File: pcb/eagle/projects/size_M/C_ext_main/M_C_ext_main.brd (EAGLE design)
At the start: 12 parts, among them U1 CP2104-F03-GM

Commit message: PCB M.1
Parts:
- added C.R3, C.R4: 0, rcl:R0603
- moved C.J2 0.29 mm to (1.64, 12.8)
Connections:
- net PROG: now also C.R4.1, C.R4.2
- net RESET: now also C.R3.1, C.R3.2
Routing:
- net PROG: track 9.97 -> 22.9 mm
- net GND: track 130.4 -> 128.3 mm
- net RX: track 5.99 -> 6.92 mm
- net VUSB: track 29.3 -> 30.1 mm
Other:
- board text added: "main M.1"
- board text removed: "ESP M.1"

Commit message: updated PCBS after the version 1 delivery
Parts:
- removed C.C4: 100n, rcl:C0603
- added C.R5: 5K1, rcl:R0603
- added C.R6: 5k1, rcl:R0603
- C.C5: value 10u -> 1u
- moved C.R3 4.08 mm to (14.9, 5.41)
- moved C.R2 3.87 mm to (3.90, 8.98)
- moved C.R1 2.03 mm to (3.87, 5.49)
- moved C.C5 1.82 mm to (3.95, 12.5)
- moved U1 1.78 mm to (11.1, 8.72)
- moved C.R4 1.11 mm to (7.86, 4.56)
- moved C.C2 0.44 mm to (17.2, 9.79)
- moved C.C3 0.14 mm to (18.7, 2.95)
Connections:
- removed net VIO: U1.5
- new net N$3: C.R6.2, U$1.A5
- new net N$4: C.R5.2, U$1.B5
- net GND: now also C.R5.1, C.R6.1; no longer C.C4.1
- net N$1: now also U$1.B7
- net N$2: now also U$1.B6
- net VCC: now also U1.5
- net VUSB: no longer C.C4.2
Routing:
- net N$2: track 2.25 -> 11.1 mm
- net VUSB: track 30.1 -> 38.7 mm
- net N$1: track 2.26 -> 9.99 mm, vias 0 -> 2
- net VCC: track 53.2 -> 46.2 mm
- net GND: track 128.3 -> 123.7 mm, vias 5 -> 9
- net N$3: track 0.00 -> 3.89 mm
- net N$4: track 0.00 -> 2.70 mm
- net SDA: track 6.33 -> 5.20 mm
- net RX: track 6.92 -> 5.81 mm
- net PROG: track 22.9 -> 24.0 mm
- net SCL: track 4.93 -> 5.89 mm
- net RESET: track 11.8 -> 12.7 mm
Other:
- board text added: "main M.2"
- board text removed: "main M.1"

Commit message: updated PCBs for version 2
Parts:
- added C.F1, C.F2: (no value), rcl:R0805
- added PROGRAMMING: TPB1,27, testpad:B1,27
- moved C.C2 4.30 mm to (14.9, 6.15)
- moved C.R3 3.91 mm to (11.1, 4.57)
- moved C.C1 0.76 mm to (19.0, 2.98)
- moved C.R5 0.38 mm to (13.1, 12.1)
- moved C.C3 0.33 mm to (18.7, 2.62)
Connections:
- new net N$5: C.F2.2, JP1.3
- new net N$6: C.F1.2, JP1.1
- new net N$7: PROGRAMMING.TP, U1.9
- net VCC: now also C.F2.1; no longer JP1.3
- net VUSB: now also C.F1.1; no longer JP1.1
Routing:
- net GND: track 123.7 -> 128.9 mm, vias 9 -> 8
- net VCC: track 46.2 -> 43.4 mm, vias 0 -> 2
- net N$6: track 0.00 -> 2.74 mm
- net N$5: track 0.00 -> 2.67 mm
- net VUSB: track 38.7 -> 36.0 mm
- net N$7: track 0.00 -> 1.62 mm
- net RESET: track 12.7 -> 11.2 mm

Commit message: closed PCB version M.2
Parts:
- renumbered PROGRAMMING to PROG

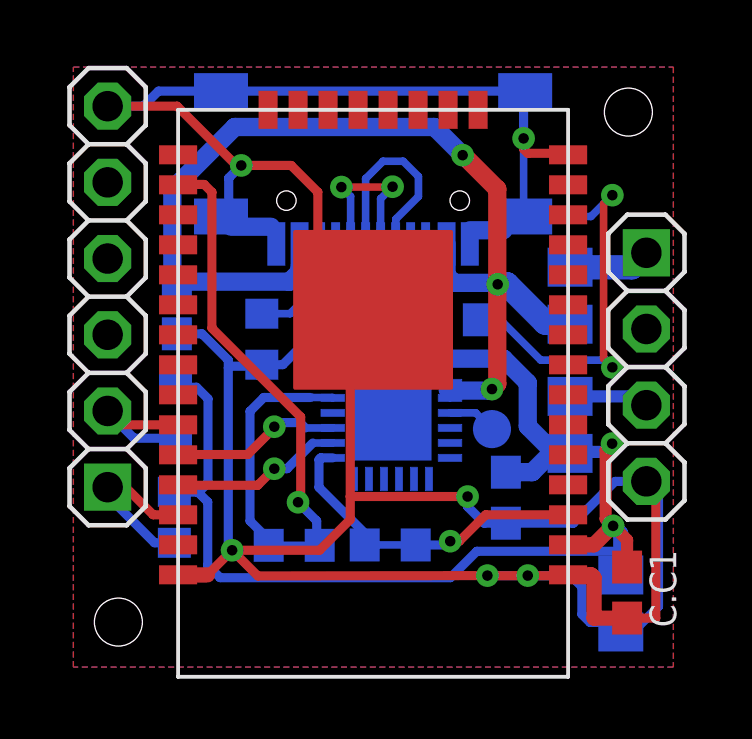
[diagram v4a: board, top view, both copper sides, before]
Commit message: updated main board - added 5 to 3.3V regulator becaues one in CP is too weak updated power board - added shotky diode to FET to be sure it works as expected
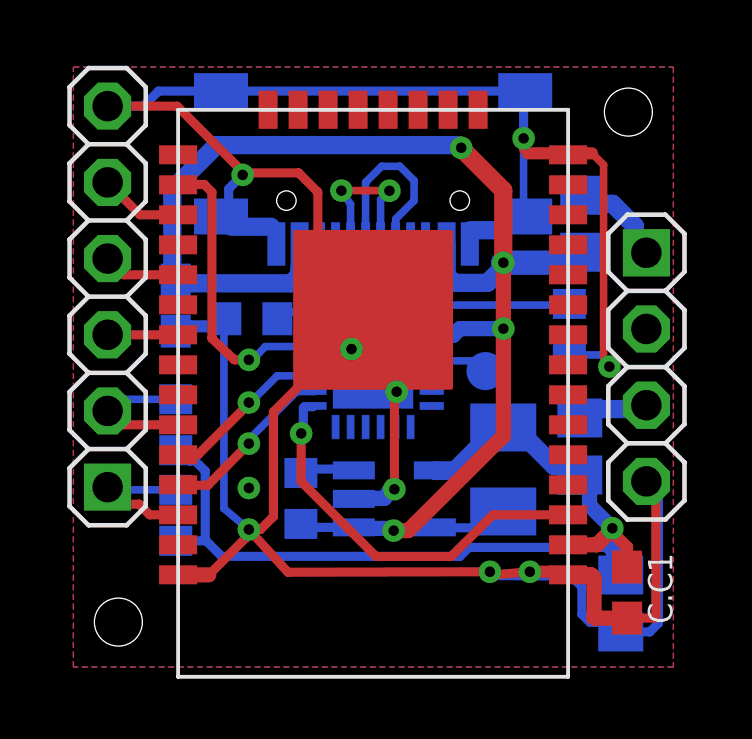
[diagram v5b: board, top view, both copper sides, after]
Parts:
- removed C.C2: 100n, rcl:C0603
- removed C.R4: 0, rcl:R0603
- removed PROG: TPB1,27, testpad:B1,27
- added D.L1: 2u2, rcl:L3230M
- added D.U2: LM3671_3.3, !stavebnice03:SOT32-5
- added P1: TPB1,27, testpad:B1,27
- C.F1, C.F2: value (none) -> 0.5A
- C.R3: value 0 -> 39k
- moved C.R5 3.91 mm to (17.0, 11.8), turned to 90 degrees
- moved C.R3 3.36 mm to (8.08, 6.12), turned to 270 degrees
- moved C.F1 2.44 mm to (17.5, 15.3)
- moved U1 1.84 mm to (10.5, 10.5)
- moved C.F2 0.79 mm to (17.4, 7.85)
- moved C.R6 0.76 mm to (6.45, 12.1), turned to 180 degrees
- moved C.R2 0.40 mm to (3.91, 8.58), turned to 270 degrees
- moved C.C5 0.10 mm to (3.91, 12.5)
- moved C.R1 0.08 mm to (3.91, 5.56), turned to 270 degrees
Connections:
- new net N$10: D.L1.1, D.U2.VOUT
- new net N$11: C.R3.1, D.U2.SHDN
- new net N$12: C.J2.5, C.U1.IO4
- new net N$13: C.J2.4, C.U1.IO17
- new net N$14: C.J2.3, C.U1.IO18
- new net N$8: U1.5, U1.6
- net GND: now also D.U2.GND; no longer C.C2.2
- net N$7: now also P1.TP; no longer PROG.TP
- net PROG: no longer C.R4.1, C.R4.2
- net RESET: no longer C.R3.1, C.R3.2
- net VCC: now also D.L1.2, D.U2.BP; no longer C.C2.1, U1.5, U1.6
- net VUSB: now also C.R3.2, D.U2.VIN
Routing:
- net PROG: track 24.0 -> 10.0 mm
- net VUSB: track 36.0 -> 47.0 mm, vias 3 -> 4
- net VCC: track 43.4 -> 33.1 mm, vias 2 -> 1
- net N$4: track 2.54 -> 6.43 mm
- net N$12: track 0.00 -> 2.80 mm
- net N$13: track 0.00 -> 2.57 mm
- net N$10: track 0.00 -> 2.54 mm
- net N$2: track 11.1 -> 8.65 mm
- net N$1: track 9.99 -> 7.57 mm
- net N$14: track 0.00 -> 2.35 mm
- net RESET: track 11.2 -> 13.4 mm
- net N$11: track 0.00 -> 1.84 mm
- net GND: track 128.9 -> 127.2 mm, vias 8 -> 10
- net SCL: track 5.89 -> 5.04 mm
- net N$8: track 0.00 -> 0.50 mm
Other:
- board text added: "main M.3"
- board text removed: "main M.2"

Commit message: PCB M.3
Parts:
- moved C.J2 0.31 mm to (1.40, 13.0)
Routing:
- net SCL: track 5.04 -> 5.66 mm
- net GND: track 127.2 -> 127.8 mm

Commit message: main and switch pcbs adjusted
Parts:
- C.R3: value 39k -> 100k
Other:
- board text added: "main M.4"
- board text removed: "main M.3"

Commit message: PCB v4
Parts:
- moved C.C5 0.10 mm to (3.81, 12.5)
- moved C.R1 0.10 mm to (3.81, 5.56)
- moved C.R2 0.10 mm to (3.81, 8.58)
- moved C.R6 0.10 mm to (6.35, 12.1)
